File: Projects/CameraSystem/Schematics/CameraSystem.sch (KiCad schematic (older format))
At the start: 0 parts

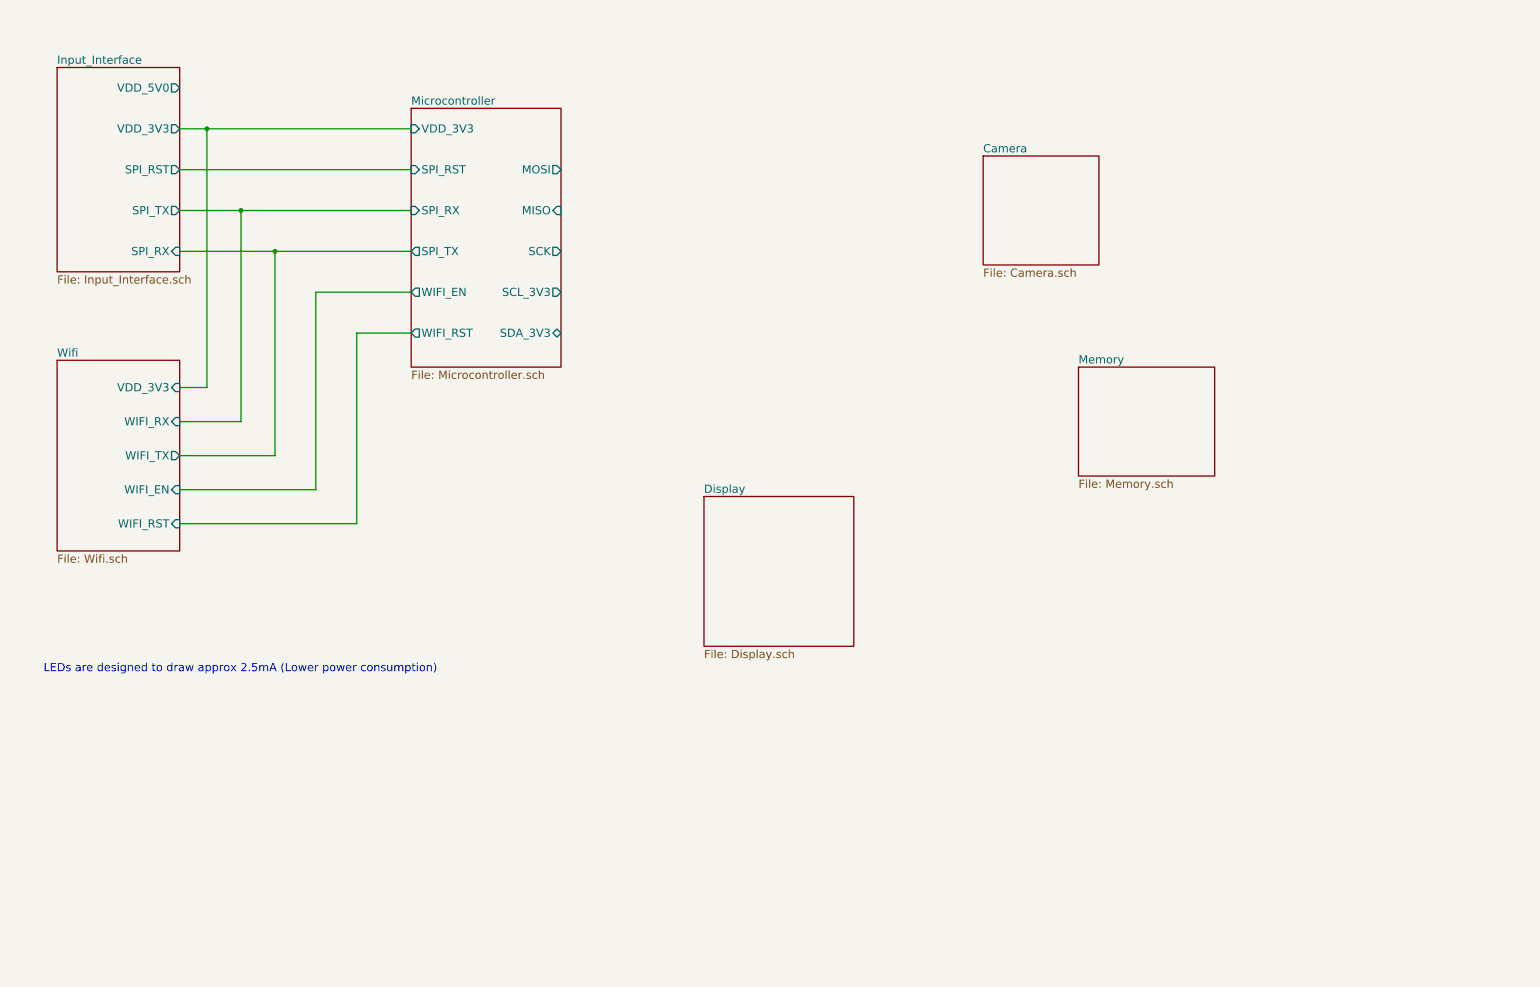
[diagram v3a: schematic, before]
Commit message: feat: first draft of uc schematic created
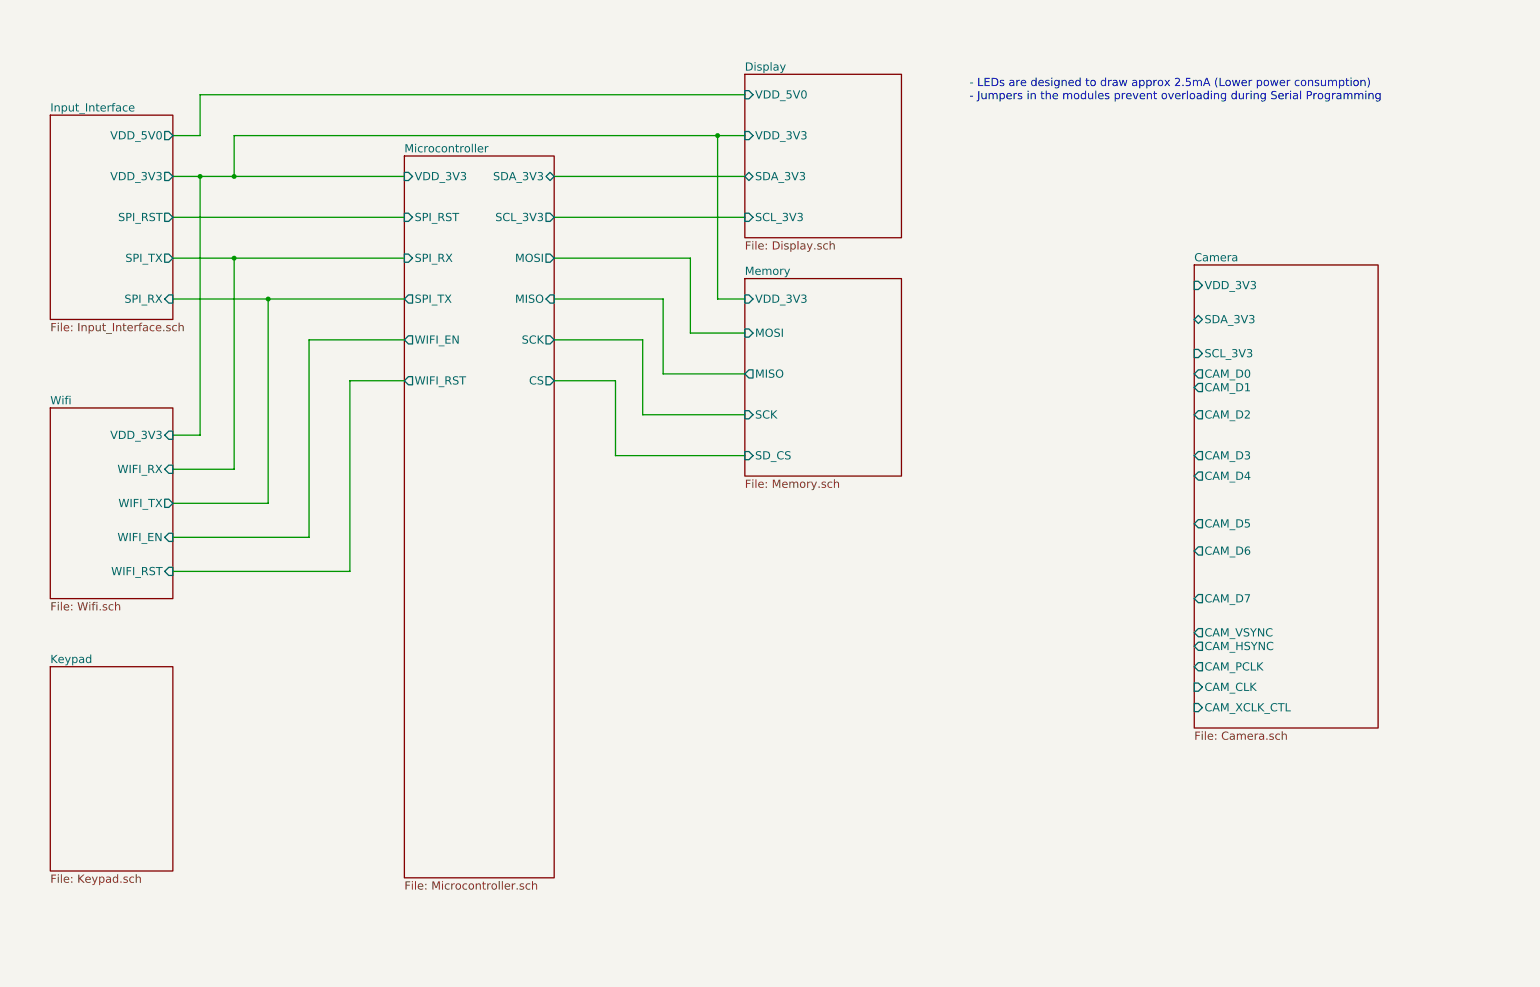
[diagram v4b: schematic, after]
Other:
- note added: "- LEDs are designed to draw approx 2.5mA (Lower power consumption)\n- Jumpers in the modules prevent overloading during Serial Programming"
- note removed: "LEDs are designed to draw approx 2.5mA (Lower power consumption)"
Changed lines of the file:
@@
 $Descr A4 11693 8268
 encoding utf-8
-Sheet 1 7
+Sheet 1 8
 Title ""
 Date ""
@@
 $EndDescr
 $Sheet
-S 1000 1000 900  1500
+S 950  1350 900  1500
 U 5BB4C1AE
 F0 "Input_Interface" 60
 F1 "Input_Interface.sch" 60
-F2 "VDD_5V0" O R 1900 1150 60
-F3 "VDD_3V3" O R 1900 1450 60
-F4 "SPI_RST" O R 1900 1750 60
-F5 "SPI_TX" O R 1900 2050 60
-F6 "SPI_RX" I R 1900 2350 60
+F2 "VDD_5V0" O R 1850 1500 60
+F3 "VDD_3V3" O R 1850 1800 60
+F4 "SPI_RST" O R 1850 2100 60
+F5 "SPI_TX" O R 1850 2400 60
+F6 "SPI_RX" I R 1850 2700 60
 $EndSheet
 $Sheet
-S 3600 1300 1100 1900
+S 3550 1650 1100 5300
 U 5BB4D99F
 F0 "Microcontroller" 60
 F1 "Microcontroller.sch" 60
-F2 "VDD_3V3" I L 3600 1450 60
-F3 "SPI_RST" I L 3600 1750 60
-F4 "SPI_TX" O L 3600 2350 60
-F5 "SPI_RX" I L 3600 2050 60
-F6 "MOSI" O R 4700 1750 60
-F7 "MISO" I R 4700 2050 60
-F8 "SCK" O R 4700 2350 60
-F9 "WIFI_EN" O L 3600 2650 60
-F10 "WIFI_RST" O L 3600 2950 60
-F11 "SCL_3V3" O R 4700 2650 60
-F12 "SDA_3V3" B R 4700 2950 60
+F2 "VDD_3V3" I L 3550 1800 60
+F3 "SPI_RST" I L 3550 2100 60
+F4 "SPI_TX" O L 3550 2700 60
+F5 "SPI_RX" I L 3550 2400 60
+F6 "MOSI" O R 4650 2400 60
+F7 "MISO" I R 4650 2700 60
+F8 "SCK" O R 4650 3000 60
+F9 "WIFI_EN" O L 3550 3000 60
+F10 "WIFI_RST" O L 3550 3300 60
+F11 "SCL_3V3" O R 4650 2100 60
+F12 "SDA_3V3" B R 4650 1800 60
+F13 "CS" O R 4650 3300 60
 $EndSheet
 $Sheet
-S 1000 3150 900  1400
+S 950  3500 900  1400
 U 5BB4D9C1
 F0 "Wifi" 60
 F1 "Wifi.sch" 60
-F2 "VDD_3V3" I R 1900 3350 60
-F3 "WIFI_TX" O R 1900 3850 60
-F4 "WIFI_RX" I R 1900 3600 60
-F5 "WIFI_RST" I R 1900 4350 60
-F6 "WIFI_EN" I R 1900 4100 60
+F2 "VDD_3V3" I R 1850 3700 60
+F3 "WIFI_TX" O R 1850 4200 60
+F4 "WIFI_RX" I R 1850 3950 60
+F5 "WIFI_RST" I R 1850 4700 60
+F6 "WIFI_EN" I R 1850 4450 60
 $EndSheet
 $Sheet
-S 8500 3200 1000 800
+S 6050 2550 1150 1450
 U 5BB4DA56
 F0 "Memory" 60
 F1 "Memory.sch" 60
+F2 "VDD_3V3" I L 6050 2700 60
+F3 "MOSI" I L 6050 2950 60
+F4 "SCK" I L 6050 3550 60
+F5 "SD_CS" I L 6050 3850 60
+F6 "MISO" O L 6050 3250 60
 $EndSheet
 $Sheet
-S 7800 1650 850  800
+S 9350 2450 1350 3400
 U 5BB4DA63
 F0 "Camera" 60
 F1 "Camera.sch" 60
+F2 "VDD_3V3" I L 9350 2600 60
+F3 "SDA_3V3" B L 9350 2850 60
+F4 "SCL_3V3" I L 9350 3100 60
+F5 "CAM_D1" O L 9350 3350 60
+F6 "CAM_D3" O L 9350 3850 60
+F7 "CAM_D5" O L 9350 4350 60
+F8 "CAM_D7" O L 9350 4900 60
+F9 "CAM_VSYNC" O L 9350 5150 60
+F10 "CAM_PCLK" O L 9350 5400 60
+F11 "CAM_D0" O L 9350 3250 60
+F12 "CAM_D2" O L 9350 3550 60
+F13 "CAM_D4" O L 9350 4000 60
+F14 "CAM_D6" O L 9350 4550 60
+F15 "CAM_HSYNC" O L 9350 5250 60
+F16 "CAM_CLK" I L 9350 5550 60
+F17 "CAM_XCLK_CTL" I L 9350 5700 60
 $EndSheet
-Text Notes 900  5450 0    60   ~ 0
-LEDs are designed to draw approx 2.5mA (Lower power consumption)
+Text Notes 7700 1250 0    60   ~ 0
+- LEDs are designed to draw approx 2.5mA (Lower power consumption)\n- Jumpers in the modules prevent overloading during Serial Programming
 Wire Wire Line
-	3600 1450 1900 1450
+	1850 1800 2050 1800
 Wire Wire Line
-	1900 1750 3600 1750
+	2050 1800 2300 1800
 Wire Wire Line
-	1900 2050 3600 2050
+	2300 1800 3550 1800
 Wire Wire Line
-	1900 2350 3600 2350
+	1850 2100 3550 2100
 Wire Wire Line
-	1900 3350 2100 3350
+	1850 2400 2300 2400
 Wire Wire Line
-	2100 3350 2100 1450
-Connection ~ 2100 1450
+	2300 2400 3550 2400
 Wire Wire Line
-	1900 3600 2350 3600
+	1850 2700 2550 2700
 Wire Wire Line
-	2350 3600 2350 2050
-Connection ~ 2350 2050
+	2550 2700 3550 2700
 Wire Wire Line
-	1900 3850 2600 3850
+	1850 3700 2050 3700
 Wire Wire Line
-	2600 3850 2600 2350
-Connection ~ 2600 2350
+	2050 3700 2050 1800
+Connection ~ 2050 1800
 Wire Wire Line
-	1900 4100 2900 4100
+	1850 3950 2300 3950
 Wire Wire Line
-	2900 4100 2900 2650
+	2300 3950 2300 2400
+Connection ~ 2300 2400
 Wire Wire Line
-	2900 2650 3600 2650
+	1850 4200 2550 4200
 Wire Wire Line
-	1900 4350 3200 4350
+	2550 4200 2550 2700
+Connection ~ 2550 2700
 Wire Wire Line
-	3200 4350 3200 2950
+	1850 4450 2850 4450
 Wire Wire Line
-	3200 2950 3600 2950
+	2850 4450 2850 3000
+Wire Wire Line
+	2850 3000 3550 3000
+Wire Wire Line
+	1850 4700 3150 4700
+Wire Wire Line
+	3150 4700 3150 3300
+Wire Wire Line
+	3150 3300 3550 3300
+Wire Wire Line
+	2300 1800 2300 1500
+Wire Wire Line
+	2300 1500 5850 1500
+Wire Wire Line
+	5850 1500 6050 1500
+Connection ~ 2300 1800
+Wire Wire Line
+	1850 1500 2050 1500
+Wire Wire Line
+	2050 1500 2050 1200
+Wire Wire Line
+	2050 1200 6050 1200
+Wire Wire Line
+	4650 1800 6050 1800
+Wire Wire Line
+	4650 2100 6050 2100
 $Sheet
-S 5750 4150 1100 1100
+S 6050 1050 1150 1200
 U 5BB9CC6E
 F0 "Display" 60
 F1 "Display.sch" 60
+F2 "VDD_5V0" I L 6050 1200 60
+F3 "VDD_3V3" I L 6050 1500 60
+F4 "SDA_3V3" B L 6050 1800 60
+F5 "SCL_3V3" I L 6050 2100 60
+$EndSheet
+Wire Wire Line
+	5850 1500 5850 2700
+Wire Wire Line
+	5850 2700 6050 2700
+Connection ~ 5850 1500
+Wire Wire Line
+	4650 2400 5650 2400
+Wire Wire Line
+	5650 2400 5650 2950
+Wire Wire Line
+	4650 2700 5450 2700
+Wire Wire Line
+	5450 2700 5450 3250
+Wire Wire Line
+	4650 3000 5300 3000
+Wire Wire Line
+	5300 3000 5300 3550
+Wire Wire Line
+	5650 2950 6050 2950
+Wire Wire Line
+	5450 3250 6050 3250
+Wire Wire Line
+	5300 3550 6050 3550
+Wire Wire Line
+	4650 3300 5100 3300
+Wire Wire Line
+	5100 3300 5100 3850
+Wire Wire Line
+	5100 3850 6050 3850
+$Sheet
+S 950  5400 900  1500
+U 5BBB389E
+F0 "Keypad" 60
+F1 "Keypad.sch" 60
 $EndSheet
 $EndSCHEMATC

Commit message: feat: add keypad schematic
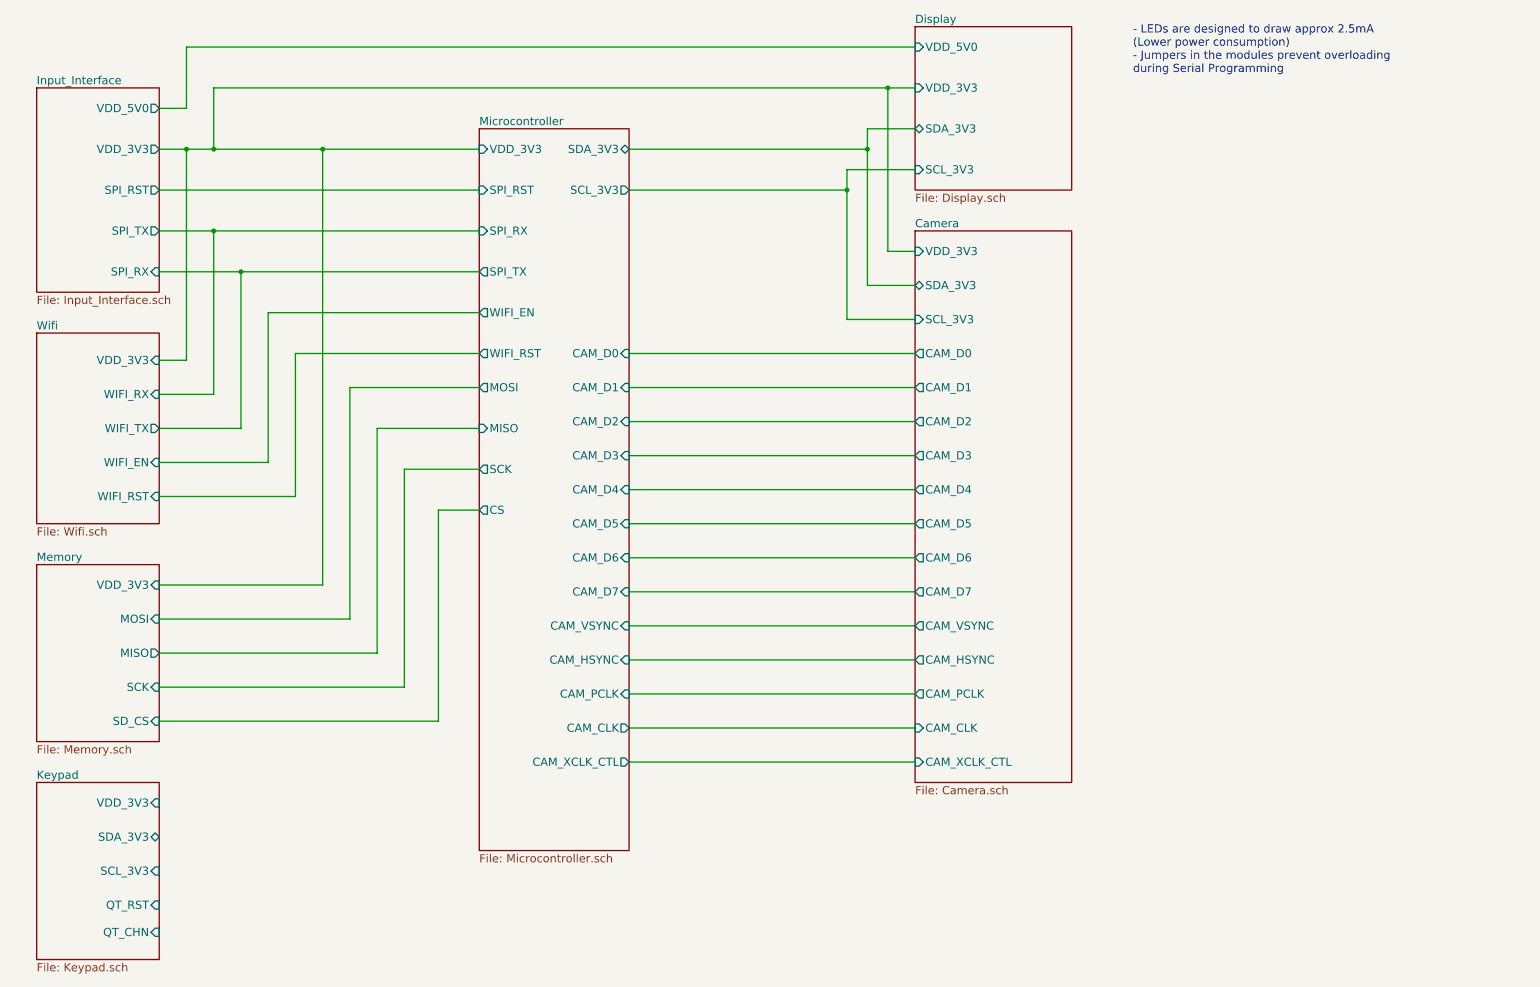
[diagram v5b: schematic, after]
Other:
- note added: "- LEDs are designed to draw approx 2.5mA \n(Lower power consumption)\n- Jumpers in the modules prevent overloading \nduring Serial Programming"
- note removed: "- LEDs are designed to draw approx 2.5mA (Lower power consumption)\n- Jumpers in the modules prevent overloading during Serial Programming"

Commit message: feat: 3.3 regulator housing changed due to temperature
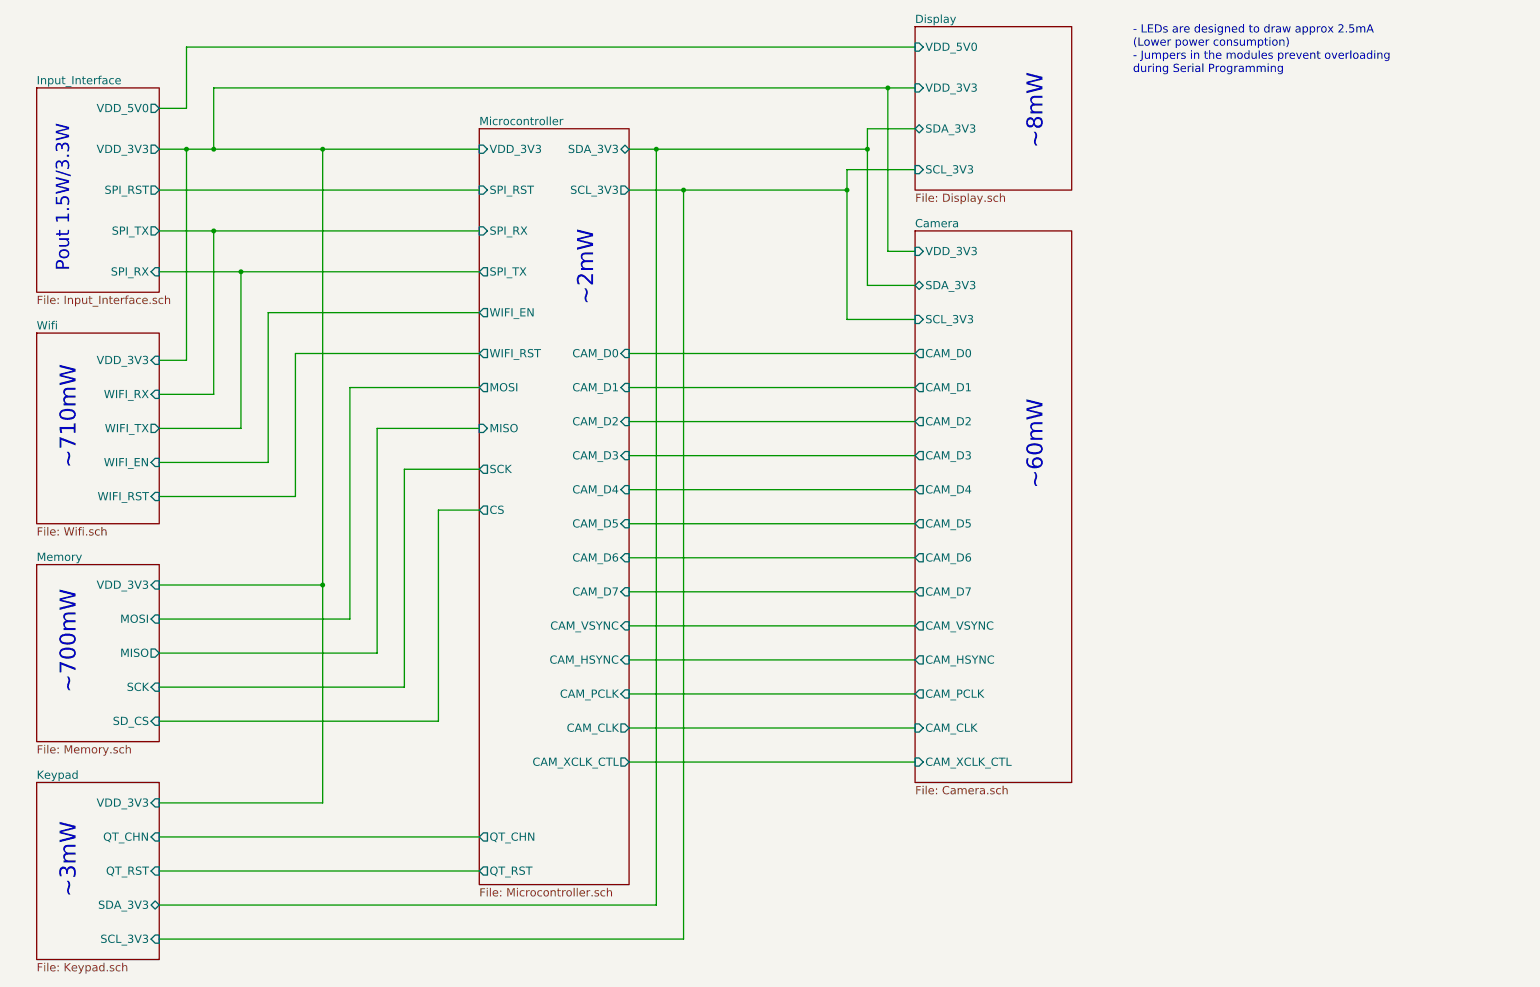
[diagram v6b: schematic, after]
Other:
- note added: "Pout 1.5W/3.3W"
- note added: "~~2mW"
- note added: "~~3mW"
- note added: "~~60mW"
- note added: "~~700mW"
- note added: "~~710mW"
- note added: "~~8mW"
